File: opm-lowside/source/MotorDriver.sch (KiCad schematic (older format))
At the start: 55 parts, among them IC301 TMC6100-LA, Q301 YJG95G06A, Q302 YJG95G06A, Q303 YJG95G06A, Q304 YJG95G06A, Q305 YJG95G06A, Q306 YJG95G06A, U1 INA180A3IDBVR, U2 INA180A3IDBVR, U3 INA180A3IDBVR

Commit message: add initial
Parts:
- removed Q301, Q302, Q303, Q304, Q305, Q306: YJG95G06A, Package_TO_SOT_SMD:TDSON-8-1, symbol opm-lowside-rescue:YJG95G06A-Transistor_FET-opm-v1.1-rescue
- added Q? (x6): HYG025N06LS1C2, Libraries:PDFN-8, symbol opm-cache:HYG025N06LS1C2
- renumbered C315 to C10, C306 to C11, C305 to C12, C307 to C13, C303 to C14, C310 to C15, C318 to C16, C304 to C17, C314 to C18, C319 to C19, C4 to C20, C5 to C21, C6 to C22, C1 to C23, C2 to C24, C3 to C25, C7 to C26, C8 to C27, C9 to C28, C311 to C7, C312 to C8, C313 to C9, R311 to R10, R314 to R11, R304 to R12, R306 to R13, R310 to R14, R313 to R15, R318 to R16, R320 to R17, R1 to R18, R2 to R19, R3 to R20, R4 to R21, R5 to R22, R6 to R23, R7 to R24, R8 to R25, R9 to R26, R10 to R27, R11 to R28, R12 to R29, R13 to R30, R14 to R31, R15 to R32, U1 to U3, U2 to U4, U3 to U5

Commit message: first config
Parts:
- IC1: renamed from U3; footprint SOT95P280X145-5N:SOT95P280X145-5N -> Libraries:SOT95P280X145-5N
- IC2: renamed from U4; footprint SOT95P280X145-5N:SOT95P280X145-5N -> Libraries:SOT95P280X145-5N
- IC3: renamed from U5; footprint SOT95P280X145-5N:SOT95P280X145-5N -> Libraries:SOT95P280X145-5N
- IC4: renamed from IC301; footprint Trinamic:QFN-44-1EP_7x7mm_P0.5mm_EP4x4mm -> Libraries:TMC6100-LA; manf_num (none) -> TMC6100-LA
- gave numbers to parts that had none: 6
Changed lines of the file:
@@
 P 3950 3500
 AR Path="/5D604226" Ref="IC?"  Part="1"
-AR Path="/5D5FDD98/5D604226" Ref="IC301"  Part="1"
-F 0 "IC301" H 3950 3550 40  0000 C CNN
+AR Path="/5D5FDD98/5D604226" Ref="IC4"  Part="1"
+F 0 "IC4" H 3950 3550 40  0000 C CNN
 F 1 "TMC6100-LA" H 3950 3450 40  0000 C CNN
-F 2 "Trinamic:QFN-44-1EP_7x7mm_P0.5mm_EP4x4mm" H 3950 3250 40  0001 C CNN
+F 2 "Libraries:TMC6100-LA" H 3950 3250 40  0001 C CNN
 F 3 "https://www.trinamic.com/fileadmin/assets/Products/ICs_Documents/TMC6200_datasheet_Rev1.04.pdf" H 3950 4325 40  0001 C CNN
+F 4 "TMC6100-LA" H 3950 3500 50  0001 C CNN "manf_num"
 	1    3950 3500
 	1    0    0    -1
@@
 	10600 4050 10600 4150
 $Comp
-L amplifier:INA180A3IDBVR U4
+L amplifier:INA180A3IDBVR IC2
 U 1 1 61DF6C56
 P 9200 3850
-F 0 "U4" H 9200 4420 50  0000 C CNN
+F 0 "IC2" H 9200 4420 50  0000 C CNN
 F 1 "INA180A3IDBVR" H 9200 4329 50  0000 C CNN
-F 2 "SOT95P280X145-5N:SOT95P280X145-5N" H 9200 3850 50  0001 L BNN
+F 2 "Libraries:SOT95P280X145-5N" H 9200 3850 50  0001 L BNN
 F 3 "https://datasheet.lcsc.com/lcsc/1811151640_Texas-Instruments-INA180A3IDBVR_C122882.pdf" H 9200 3850 50  0001 L BNN
 F 4 "C122882" H 9200 3850 50  0001 C CNN "LCSC"
@@
 	10450 5750 10600 5750
 $Comp
-L amplifier:INA180A3IDBVR U5
+L amplifier:INA180A3IDBVR IC3
 U 1 1 61E59F21
 P 9200 5850
-F 0 "U5" H 9200 6420 50  0000 C CNN
+F 0 "IC3" H 9200 6420 50  0000 C CNN
 F 1 "INA180A3IDBVR" H 9200 6329 50  0000 C CNN
-F 2 "SOT95P280X145-5N:SOT95P280X145-5N" H 9200 5850 50  0001 L BNN
+F 2 "Libraries:SOT95P280X145-5N" H 9200 5850 50  0001 L BNN
 F 3 "https://datasheet.lcsc.com/lcsc/1811151640_Texas-Instruments-INA180A3IDBVR_C122882.pdf" H 9200 5850 50  0001 L BNN
 F 4 "C122882" H 9200 5850 50  0001 C CNN "LCSC"
@@
 	8000 1700 8350 1700
 $Comp
-L amplifier:INA180A3IDBVR U3
+L amplifier:INA180A3IDBVR IC1
 U 1 1 61D23CA5
 P 9200 1900
-F 0 "U3" H 9200 2470 50  0000 C CNN
+F 0 "IC1" H 9200 2470 50  0000 C CNN
 F 1 "INA180A3IDBVR" H 9200 2379 50  0000 C CNN
-F 2 "SOT95P280X145-5N:SOT95P280X145-5N" H 9200 1900 50  0001 L BNN
+F 2 "Libraries:SOT95P280X145-5N" H 9200 1900 50  0001 L BNN
 F 3 "https://datasheet.lcsc.com/lcsc/1811151640_Texas-Instruments-INA180A3IDBVR_C122882.pdf" H 9200 1900 50  0001 L BNN
 F 4 "C122882" H 9200 1900 50  0001 C CNN "LCSC"
@@
 	10600 6050 10600 6150
 $Comp
-L opm-cache:HYG025N06LS1C2 Q?
+L opm-cache:HYG025N06LS1C2 Q2
 U 1 1 61CA9BEB
 P 6900 1400
-F 0 "Q?" H 7100 1438 39  0000 L CNN
+F 0 "Q2" H 7100 1438 39  0000 L CNN
 F 1 "HYG025N06LS1C2" H 7100 1363 39  0000 L CNN
 F 2 "Libraries:PDFN-8" H 7000 1400 39  0001 L CIN
@@
 $EndComp
 $Comp
-L opm-cache:HYG025N06LS1C2 Q?
+L opm-cache:HYG025N06LS1C2 Q1
 U 1 1 61CABB70
 P 6900 800
-F 0 "Q?" H 7100 838 39  0000 L CNN
+F 0 "Q1" H 7100 838 39  0000 L CNN
 F 1 "HYG025N06LS1C2" H 7100 763 39  0000 L CNN
 F 2 "Libraries:PDFN-8" H 7000 800 39  0001 L CIN
@@
 $EndComp
 $Comp
-L opm-cache:HYG025N06LS1C2 Q?
+L opm-cache:HYG025N06LS1C2 Q3
 U 1 1 61CACBB5
 P 6900 2750
-F 0 "Q?" H 7100 2788 39  0000 L CNN
+F 0 "Q3" H 7100 2788 39  0000 L CNN
 F 1 "HYG025N06LS1C2" H 7100 2713 39  0000 L CNN
 F 2 "Libraries:PDFN-8" H 7000 2750 39  0001 L CIN
@@
 $EndComp
 $Comp
-L opm-cache:HYG025N06LS1C2 Q?
+L opm-cache:HYG025N06LS1C2 Q4
 U 1 1 61CAE7A7
 P 6900 3350
-F 0 "Q?" H 7100 3388 39  0000 L CNN
+F 0 "Q4" H 7100 3388 39  0000 L CNN
 F 1 "HYG025N06LS1C2" H 7100 3313 39  0000 L CNN
 F 2 "Libraries:PDFN-8" H 7000 3350 39  0001 L CIN
@@
 $EndComp
 $Comp
-L opm-cache:HYG025N06LS1C2 Q?
+L opm-cache:HYG025N06LS1C2 Q5
 U 1 1 61CAF7AF
 P 6900 4750
-F 0 "Q?" H 7100 4788 39  0000 L CNN
+F 0 "Q5" H 7100 4788 39  0000 L CNN
 F 1 "HYG025N06LS1C2" H 7100 4713 39  0000 L CNN
 F 2 "Libraries:PDFN-8" H 7000 4750 39  0001 L CIN
@@
 $EndComp
 $Comp
-L opm-cache:HYG025N06LS1C2 Q?
+L opm-cache:HYG025N06LS1C2 Q6
 U 1 1 61CB0C32
 P 6900 5350
-F 0 "Q?" H 7100 5388 39  0000 L CNN
+F 0 "Q6" H 7100 5388 39  0000 L CNN
 F 1 "HYG025N06LS1C2" H 7100 5313 39  0000 L CNN
 F 2 "Libraries:PDFN-8" H 7000 5350 39  0001 L CIN

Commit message: update parts
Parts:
- C14, C15: LCSC C519409 -> C106243; manf_num CC0603KRX7R7BB471 -> CC0805KKX7R0BB104
- C16: Field4 C519409 -> C106243; Field5 CC0603KRX7R7BB471 -> CC0805KKX7R0BB104
- C17: value 2,2μF/100V -> 2.2μF/100V; LCSC (none) -> C412614; manf_num   (none) -> HMJ325AB7225KMHP
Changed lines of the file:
@@
 P 7400 850
 F 0 "C17" V 7250 850 39  0000 C CNN
-F 1 "2,2μF/100V" V 7550 850 39  0000 C CNN
+F 1 "2.2μF/100V" V 7550 850 39  0000 C CNN
 F 2 "Capacitor_SMD:C_1210_3225Metric" H 7438 700 39  0001 C CNN
-F 3 "~" H 7400 850 39  0001 C CNN
+F 3 "https://datasheet.lcsc.com/lcsc/1912111437_Taiyo-Yuden-HMJ325AB7225KMHP_C412614.pdf" H 7400 850 39  0001 C CNN
+F 4 "C412614" V 7400 850 50  0001 C CNN "LCSC"
+F 5 "HMJ325AB7225KMHP" V 7400 850 50  0001 C CNN "manf_num  "
 	1    7400 850
 	1    0    0    -1
@@
 F 1 "470nF/16V" V 5700 1050 39  0000 C CNN
 F 2 "Capacitor_SMD:C_0603_1608Metric" H 5588 900 39  0001 C CNN
-F 3 "https://www.mouser.fi/datasheet/2/447/yago_s_a0011723860_1-2286802.pdf" H 5550 1050 39  0001 C CNN
-F 4 "C519409" V 5550 1050 50  0001 C CNN "LCSC"
-F 5 "CC0603KRX7R7BB471" V 5550 1050 50  0001 C CNN "manf_num"
+F 3 "https://datasheet.lcsc.com/lcsc/1811082118_YAGEO-CC0603KRX7R7BB474_C106851.pdf" H 5550 1050 39  0001 C CNN
+F 4 "C106243" V 5550 1050 50  0001 C CNN "LCSC"
+F 5 "CC0805KKX7R0BB104" V 5550 1050 50  0001 C CNN "manf_num"
 F 6 "CC0603JRX7R7BB471" V 5550 1050 50  0001 C CNN "alt"
 	1    5550 1050
@@
 F 1 "470nF/16V" V 5700 3000 39  0000 C CNN
 F 2 "Capacitor_SMD:C_0603_1608Metric" H 5588 2850 39  0001 C CNN
-F 3 "https://www.mouser.fi/datasheet/2/447/yago_s_a0011723860_1-2286802.pdf" H 5550 3000 39  0001 C CNN
-F 4 "C519409" V 5550 3000 50  0001 C CNN "LCSC"
-F 5 "CC0603KRX7R7BB471" V 5550 3000 50  0001 C CNN "manf_num"
+F 3 "https://datasheet.lcsc.com/lcsc/1811082118_YAGEO-CC0603KRX7R7BB474_C106851.pdf" H 5550 3000 39  0001 C CNN
+F 4 "C106243" V 5550 3000 50  0001 C CNN "LCSC"
+F 5 "CC0805KKX7R0BB104" V 5550 3000 50  0001 C CNN "manf_num"
 F 6 "CC0603JRX7R7BB471" V 5550 3000 50  0001 C CNN "alt"
 	1    5550 3000
@@
 F 1 "470nF/16V" V 5700 5000 39  0000 C CNN
 F 2 "Capacitor_SMD:C_0603_1608Metric" H 5588 4850 39  0001 C CNN
-F 3 "https://www.mouser.fi/datasheet/2/447/yago_s_a0011723860_1-2286802.pdf" H 5550 5000 39  0001 C CNN
-F 4 "C519409" V 5550 5000 50  0001 C CNN "Field4"
-F 5 "CC0603KRX7R7BB471" V 5550 5000 50  0001 C CNN "Field5"
+F 3 "https://datasheet.lcsc.com/lcsc/1811082118_YAGEO-CC0603KRX7R7BB474_C106851.pdf" H 5550 5000 39  0001 C CNN
+F 4 "C106243" V 5550 5000 50  0001 C CNN "Field4"
+F 5 "CC0805KKX7R0BB104" V 5550 5000 50  0001 C CNN "Field5"
 F 6 "CC0603JRX7R7BB471" V 5550 5000 50  0001 C CNN "Field6"
 	1    5550 5000

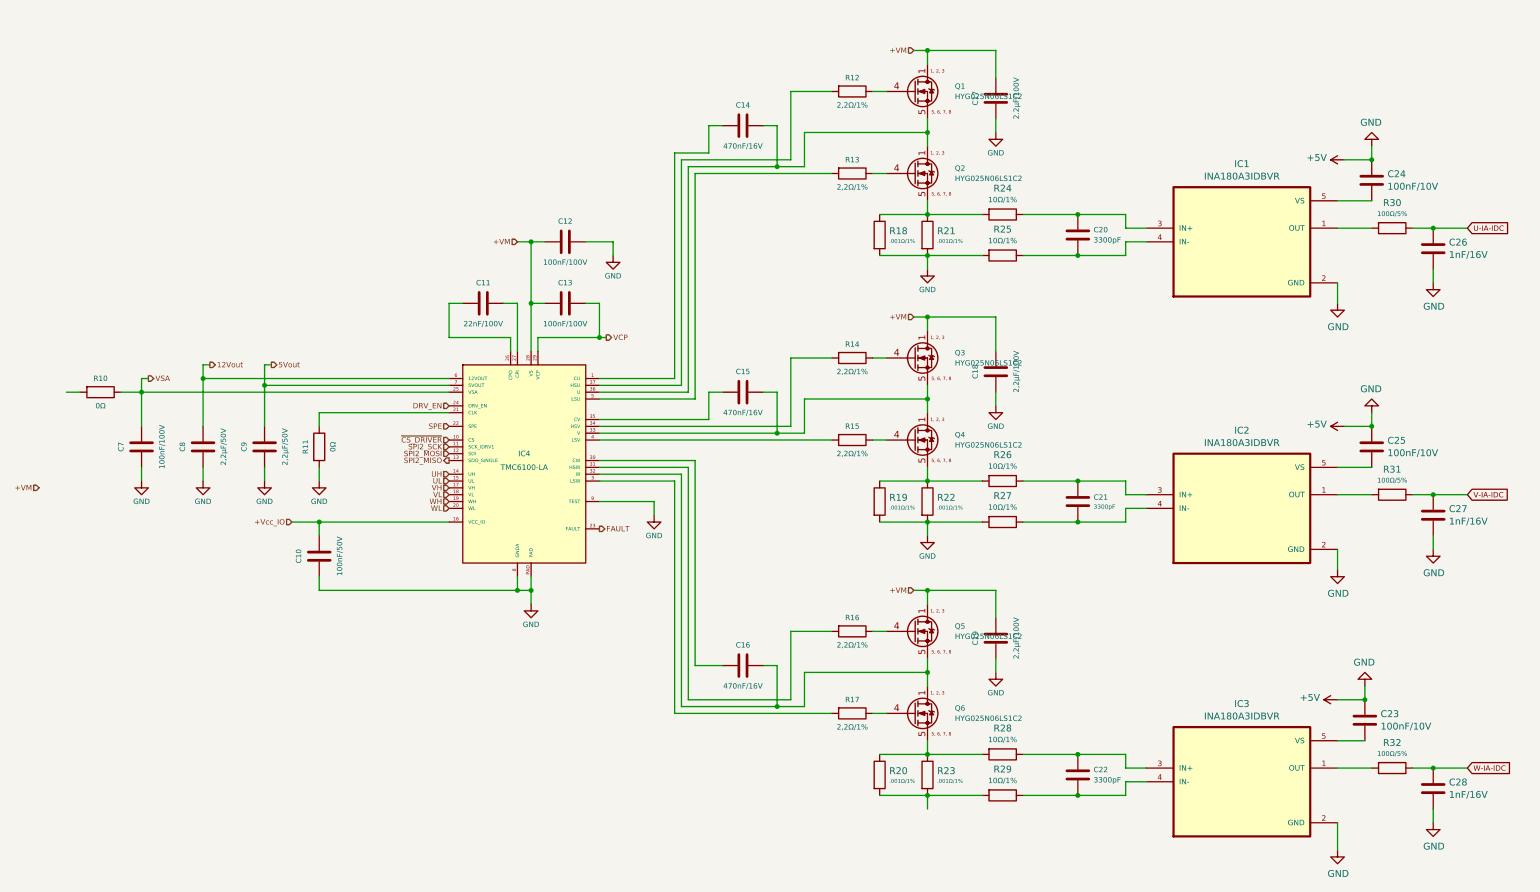
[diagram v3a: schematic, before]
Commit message: add manf num
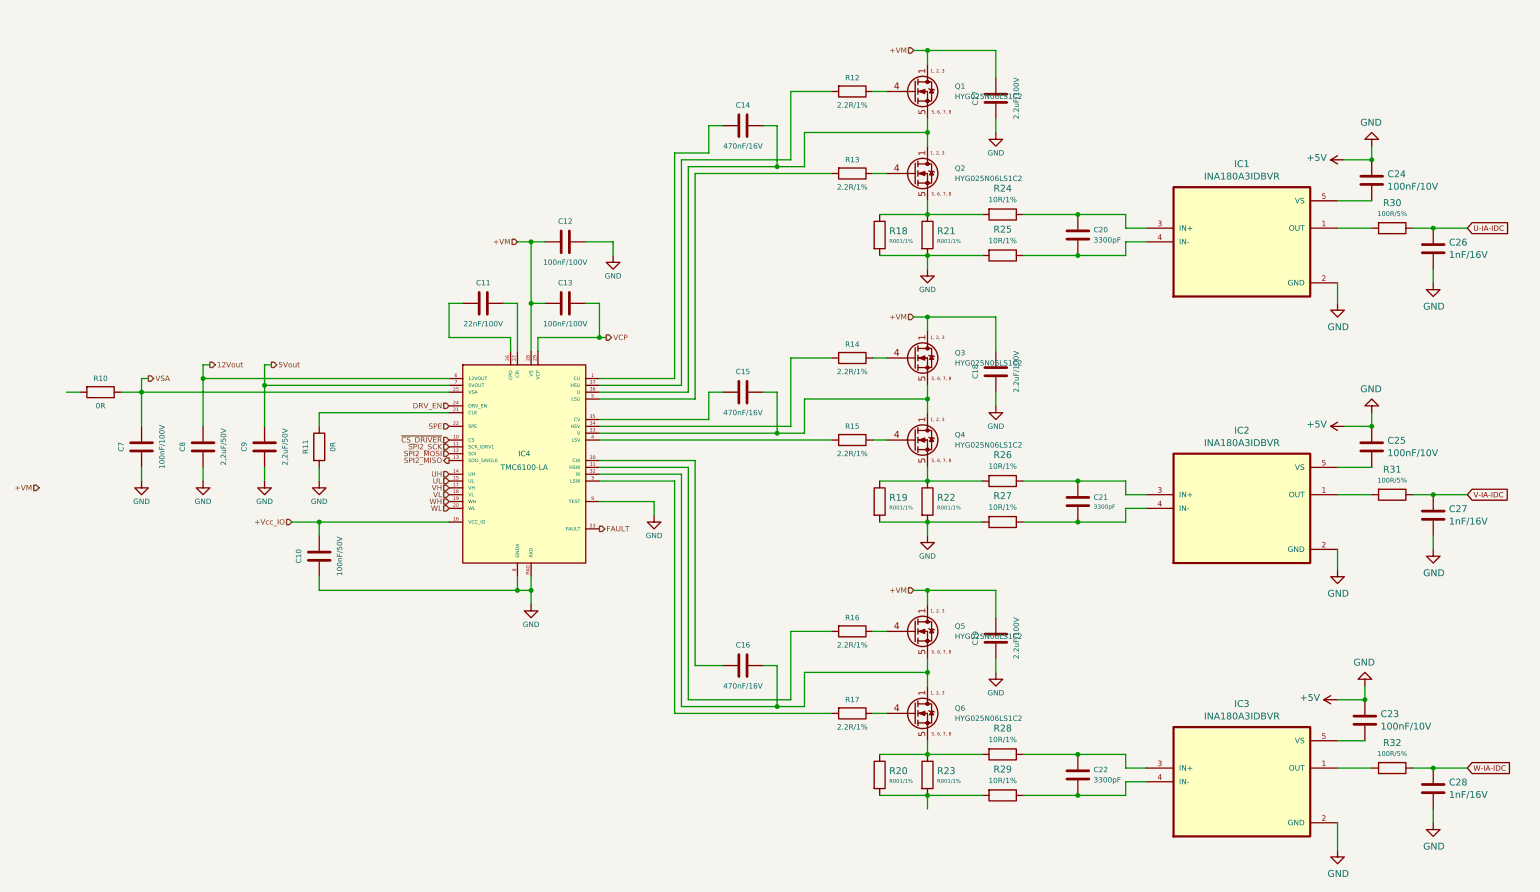
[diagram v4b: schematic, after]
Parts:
- C14, C15: LCSC C106243 -> C106851; manf_num CC0805KKX7R0BB104 -> CC0603KRX7R7BB474
- C16: Field4 C106243 -> (none); Field5 CC0805KKX7R0BB104 -> (none); Field6 CC0603JRX7R7BB471 -> (none); LCSC (none) -> C106851; manf_num (none) -> CC0603KRX7R7BB474
- C17: value 2.2μF/100V -> 2.2uF/100V
- C18, C19: value 2,2μF/100V -> 2.2uF/100V
- C20: LCSC (none) -> C1613; manf_num (none) -> CL10B332KB8NNNC
- C8, C9: value 2,2μF/50V -> 2,2uF/50V
- R10, R11: value 0Ω -> 0R
- R12, R13, R14, R15, R16, R17: value 2,2Ω/1% -> 2.2R/1%; LCSC (none) -> C22939; manf_num (none) -> 0603WAF220KT5E
- R18, R19, R20, R21, R22, R23: value .001Ω/1% -> R001/1%
- R24, R26, R27, R28, R29: value 10Ω/1% -> 10R/1%
- R25: value 10Ω/1% -> 10R/1%; LCSC (none) -> C22859; alt (none) -> AC0603FR-0710RL; manf_num (none) -> 0603WAF100JT5E
- R30, R31, R32: value 100Ω/5% -> 100R/5%

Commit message: add manf num
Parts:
- C10: Field4 C14663 -> (none); Field5 CC0603KRX7R9BB104 -> (none); LCSC (none) -> C14663; manf_num (none) -> CC0603KRX7R9BB104
- C18, C19: LCSC (none) -> C412614; manf_num (none) -> HMJ325AB7225KMHP
- C8: Field4 C49217 -> (none); LCSC (none) -> C49217
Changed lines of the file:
@@
 F 1 "2.2uF/100V" V 7550 2850 39  0000 C CNN
 F 2 "Capacitor_SMD:C_1210_3225Metric" H 7438 2700 39  0001 C CNN
-F 3 "~" H 7400 2850 39  0001 C CNN
+F 3 "https://datasheet.lcsc.com/lcsc/1912111437_Taiyo-Yuden-HMJ325AB7225KMHP_C412614.pdf" H 7400 2850 39  0001 C CNN
+F 4 "C412614" V 7400 2850 50  0001 C CNN "LCSC"
+F 5 "HMJ325AB7225KMHP" V 7400 2850 50  0001 C CNN "manf_num"
 	1    7400 2850
 	1    0    0    -1
@@
 F 1 "2.2uF/100V" V 7550 4800 39  0000 C CNN
 F 2 "Capacitor_SMD:C_1210_3225Metric" H 7438 4650 39  0001 C CNN
-F 3 "~" H 7400 4800 39  0001 C CNN
+F 3 "https://datasheet.lcsc.com/lcsc/1912111437_Taiyo-Yuden-HMJ325AB7225KMHP_C412614.pdf" H 7400 4800 39  0001 C CNN
+F 4 "C412614" V 7400 4800 50  0001 C CNN "LCSC"
+F 5 "HMJ325AB7225KMHP" V 7400 4800 50  0001 C CNN "manf_num"
 	1    7400 4800
 	1    0    0    -1
@@
 F 2 "Capacitor_SMD:C_0603_1608Metric" H 2488 4050 39  0001 C CNN
 F 3 "https://www.mouser.fi/datasheet/2/447/UPY_GPHC_X7R_6_3V_to_50V_20-1995650.pdf" H 2450 4200 39  0001 C CNN
-F 4 "C14663" V 2450 4200 50  0001 C CNN "Field4"
-F 5 "CC0603KRX7R9BB104" V 2450 4200 50  0001 C CNN "Field5"
+F 4 "C14663" V 2450 4200 50  0001 C CNN "LCSC"
+F 5 "CC0603KRX7R9BB104" V 2450 4200 50  0001 C CNN "manf_num"
 	1    2450 4200
 	1    0    0    -1
@@
 F 2 "Capacitor_SMD:C_0805_2012Metric" H 1638 3250 39  0001 C CNN
 F 3 "https://datasheet.lcsc.com/lcsc/1811101411_FH-Guangdong-Fenghua-Advanced-Tech-0805F225M500NT_C49217.pdf" H 1600 3400 39  0001 C CNN
-F 4 "C49217" V 1600 3400 50  0001 C CNN "Field4"
+F 4 "C49217" V 1600 3400 50  0001 C CNN "LCSC"
 F 5 "0805F225M500NT" V 1600 3400 50  0001 C CNN "manf_num"
 F 6 "UMK212BB7225KG-T" V 1600 3400 50  0001 C CNN "alt"

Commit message: increase caps
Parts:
- C17: value 2.2uF/100V -> 10uF/100V; footprint Capacitor_SMD:C_1210_3225Metric -> Capacitor_SMD:C_2220_5650Metric; manf_num   HMJ325AB7225KMHP -> FS55X106K101EHG
- C18: value 2.2uF/100V -> 10uF/100V; footprint Capacitor_SMD:C_1210_3225Metric -> Capacitor_SMD:C_2220_5650Metric; manf_num HMJ325AB7225KMHP -> FS55X106K101EHG
- C19: value 2.2uF/100V -> 10uF/100V; footprint Capacitor_SMD:C_1210_3225Metric -> Capacitor_SMD:C_2220_5650Metric; LCSC C412614 -> C153035; manf_num HMJ325AB7225KMHP -> FS55X106K101EHG
- C20: LCSC C1613 -> C153035
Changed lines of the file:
@@
 P 7400 850
 F 0 "C17" V 7250 850 39  0000 C CNN
-F 1 "2.2uF/100V" V 7550 850 39  0000 C CNN
-F 2 "Capacitor_SMD:C_1210_3225Metric" H 7438 700 39  0001 C CNN
-F 3 "https://datasheet.lcsc.com/lcsc/1912111437_Taiyo-Yuden-HMJ325AB7225KMHP_C412614.pdf" H 7400 850 39  0001 C CNN
+F 1 "10uF/100V" V 7550 850 39  0000 C CNN
+F 2 "Capacitor_SMD:C_2220_5650Metric" H 7438 700 39  0001 C CNN
+F 3 "https://datasheet.lcsc.com/lcsc/1811111621_PSA-Prosperity-Dielectrics-FS55X106K101EHG_C153035.pdf" H 7400 850 39  0001 C CNN
 F 4 "C412614" V 7400 850 50  0001 C CNN "LCSC"
-F 5 "HMJ325AB7225KMHP" V 7400 850 50  0001 C CNN "manf_num  "
+F 5 "FS55X106K101EHG" V 7400 850 50  0001 C CNN "manf_num  "
 	1    7400 850
 	1    0    0    -1
@@
 P 7400 2850
 F 0 "C18" V 7250 2850 39  0000 C CNN
-F 1 "2.2uF/100V" V 7550 2850 39  0000 C CNN
-F 2 "Capacitor_SMD:C_1210_3225Metric" H 7438 2700 39  0001 C CNN
-F 3 "https://datasheet.lcsc.com/lcsc/1912111437_Taiyo-Yuden-HMJ325AB7225KMHP_C412614.pdf" H 7400 2850 39  0001 C CNN
+F 1 "10uF/100V" V 7550 2850 39  0000 C CNN
+F 2 "Capacitor_SMD:C_2220_5650Metric" H 7438 2700 39  0001 C CNN
+F 3 "https://datasheet.lcsc.com/lcsc/1811111621_PSA-Prosperity-Dielectrics-FS55X106K101EHG_C153035.pdf" H 7400 2850 39  0001 C CNN
 F 4 "C412614" V 7400 2850 50  0001 C CNN "LCSC"
-F 5 "HMJ325AB7225KMHP" V 7400 2850 50  0001 C CNN "manf_num"
+F 5 "FS55X106K101EHG" V 7400 2850 50  0001 C CNN "manf_num"
 	1    7400 2850
 	1    0    0    -1
@@
 P 7400 4800
 F 0 "C19" V 7250 4800 39  0000 C CNN
-F 1 "2.2uF/100V" V 7550 4800 39  0000 C CNN
-F 2 "Capacitor_SMD:C_1210_3225Metric" H 7438 4650 39  0001 C CNN
-F 3 "https://datasheet.lcsc.com/lcsc/1912111437_Taiyo-Yuden-HMJ325AB7225KMHP_C412614.pdf" H 7400 4800 39  0001 C CNN
-F 4 "C412614" V 7400 4800 50  0001 C CNN "LCSC"
-F 5 "HMJ325AB7225KMHP" V 7400 4800 50  0001 C CNN "manf_num"
+F 1 "10uF/100V" V 7550 4800 39  0000 C CNN
+F 2 "Capacitor_SMD:C_2220_5650Metric" H 7438 4650 39  0001 C CNN
+F 3 "https://datasheet.lcsc.com/lcsc/1811111621_PSA-Prosperity-Dielectrics-FS55X106K101EHG_C153035.pdf" H 7400 4800 39  0001 C CNN
+F 4 "C153035" V 7400 4800 50  0001 C CNN "LCSC"
+F 5 "FS55X106K101EHG" V 7400 4800 50  0001 C CNN "manf_num"
 	1    7400 4800
 	1    0    0    -1
@@
 F 2 "Capacitor_SMD:C_0603_1608Metric" H 8038 1700 50  0001 C CNN
 F 3 "https://datasheet.lcsc.com/lcsc/1810261513_Samsung-Electro-Mechanics-CL10B332KB8NNNC_C1613.pdf" H 8000 1850 50  0001 C CNN
-F 4 "C1613" H 8000 1850 50  0001 C CNN "LCSC"
+F 4 "C153035" H 8000 1850 50  0001 C CNN "LCSC"
 F 5 "CL10B332KB8NNNC" H 8000 1850 50  0001 C CNN "manf_num"
 	1    8000 1850
